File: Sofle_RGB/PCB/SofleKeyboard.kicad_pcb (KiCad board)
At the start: 2 copper layers, 143.4 x 111.8 mm, 97 parts, among them J1 LED, J2 4PIN, J3 OLED, J4 key leds, J5 backlight sel, J6 indicator bypass, P1 i2c_pin, P2 i2c_pin, SW1 SW_PUSH-MX_W_LED, SW10 SW_PUSH-MX_W_LED, SW11 SW_PUSH-MX_W_LED, SW12 SW_PUSH-MX_W_LED, SW13 SW_PUSH-MX_W_LED, SW14 SW_PUSH-MX_W_LED, SW15 SW_PUSH-MX_W_LED, SW16 SW_PUSH-MX_W_LED, SW17 SW_PUSH-MX_W_LED, SW18 SW_PUSH-MX_W_LED, SW19 SW_PUSH-MX_W_LED, SW2 SW_PUSH-MX_W_LED, SW20 SW_PUSH-MX_W_LED, SW21 SW_PUSH-MX_W_LED, SW22 SW_PUSH-MX_W_LED, SW23 SW_PUSH-MX_W_LED, SW24 SW_PUSH-MX_W_LED, SW25 Rotary_Encoder_Switch, SW26 SW_PUSH-MX_W_LED, SW27 SW_PUSH-MX_W_LED, SW28 SW_PUSH-MX_W_LED, SW29 SW_PUSH-MX_W_LED, SW3 SW_PUSH-MX_W_LED, SW30 SW_PUSH-MX_W_LED, SW4 SW_PUSH-MX_W_LED, SW5 SW_PUSH-MX_W_LED, SW6 SW_PUSH-MX_W_LED, SW7 SW_PUSH-MX_W_LED, SW8 SW_PUSH-MX_W_LED, SW9 SW_PUSH-MX_W_LED, U1 ProMicro

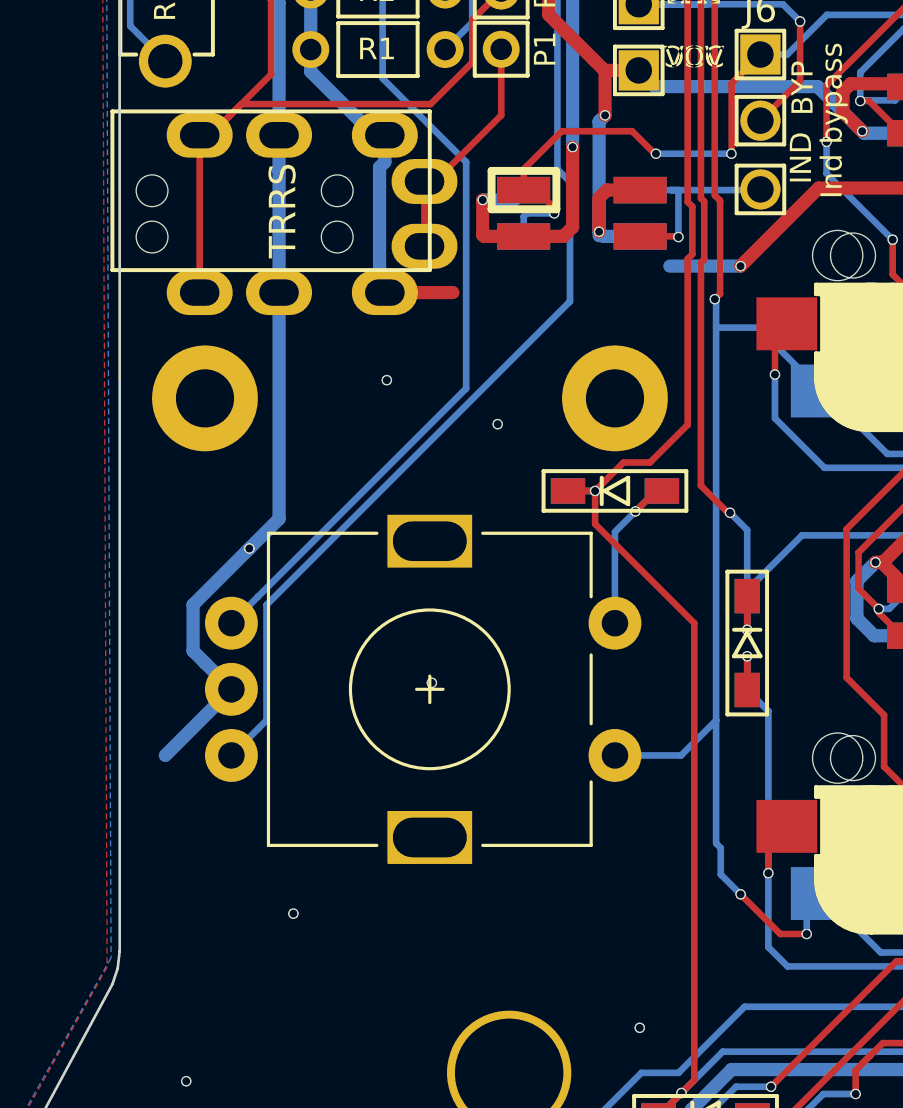
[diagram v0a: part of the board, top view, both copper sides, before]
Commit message: Added SW31 into the place where the encoder is located.
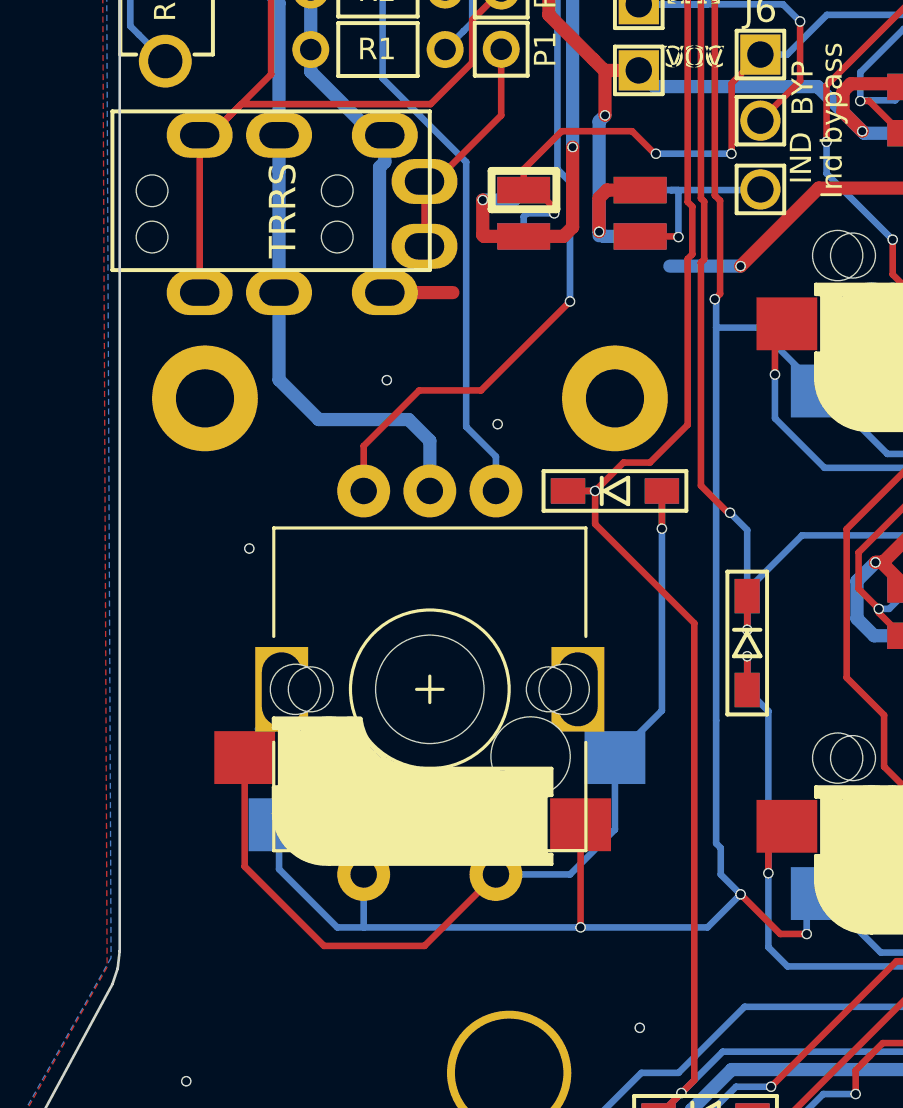
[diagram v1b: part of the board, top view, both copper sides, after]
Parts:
- added SW31: SW_PUSH-MX_W_LED, footprints:cherry_mx, F.Cu at (100.0, 104.5)
- turned SW25 to 270 degrees
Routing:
- net SW25B: track 7.11 -> 36.5 mm
- net SW25A: track 153.3 -> 175.4 mm, vias 10 -> 11
- net ENCB: track 73.5 -> 62.8 mm, vias 1 -> 2
- net GND: track 1001.1 -> 992.5 mm, vias 230 -> 228
- net ENCA: track 69.0 -> 60.7 mm
